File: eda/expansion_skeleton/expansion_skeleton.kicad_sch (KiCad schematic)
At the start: 2 parts

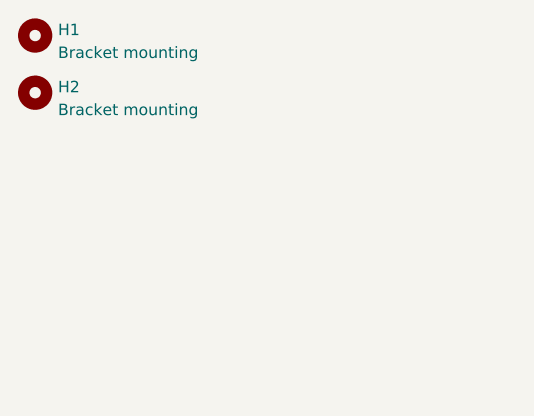
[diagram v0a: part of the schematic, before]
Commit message: EDA work for new expansion header
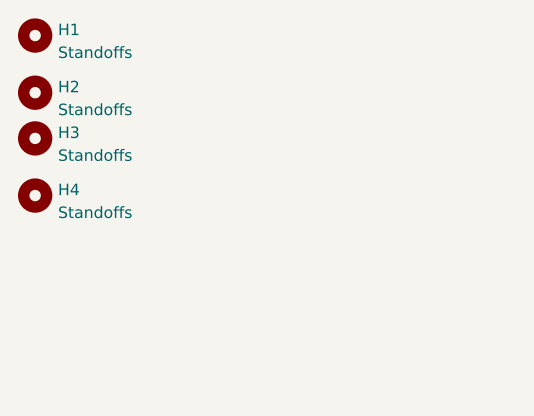
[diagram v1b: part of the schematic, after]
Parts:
- added H3, H4: Standoffs, MountingHole:MountingHole_2.5mm, symbol Mechanical:MountingHole
- H1, H2: value Bracket mounting -> Standoffs
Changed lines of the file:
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@@
 (kicad_sch (version 20230121) (generator eeschema)
   (paper "A4")
+  (symbol (lib_id "Mechanical:MountingHole") (at 21.59 34.29 0) (unit 1)
+    (in_bom yes) (on_board yes) (dnp no) (fields_autoplaced)
+    (property "Reference" "H3" (at 24.13 33.655 0)
+      (effects (font (size 1.27 1.27)) (justify left))
+    )
+    (property "Value" "Standoffs" (at 24.13 36.195 0)
+      (effects (font (size 1.27 1.27)) (justify left))
+    )
+    (property "Footprint" "MountingHole:MountingHole_2.5mm" (at 21.59 34.29 0)
+      (effects (font (size 1.27 1.27)) hide)
+    )
+    (property "Datasheet" "~" (at 21.59 34.29 0)
+      (effects (font (size 1.27 1.27)) hide)
+    )
+    (instances
+      (project "expansion_skeleton"
+        (path "/f65326c0-118f-43ae-8d7d-86cc11609fcf"
+          (reference "H3") (unit 1)
+        )
+      )
+    )
+  )
+  (symbol (lib_id "Mechanical:MountingHole") (at 21.59 40.64 0) (unit 1)
+    (in_bom yes) (on_board yes) (dnp no) (fields_autoplaced)
+    (property "Reference" "H4" (at 24.13 40.005 0)
+      (effects (font (size 1.27 1.27)) (justify left))
+    )
+    (property "Value" "Standoffs" (at 24.13 42.545 0)
+      (effects (font (size 1.27 1.27)) (justify left))
+    )
+    (property "Footprint" "MountingHole:MountingHole_2.5mm" (at 21.59 40.64 0)
+      (effects (font (size 1.27 1.27)) hide)
+    )
+    (property "Datasheet" "~" (at 21.59 40.64 0)
+      (effects (font (size 1.27 1.27)) hide)
+    )
+    (instances
+      (project "expansion_skeleton"
+        (path "/f65326c0-118f-43ae-8d7d-86cc11609fcf"
+          (reference "H4") (unit 1)
+        )
+      )
+    )
+  )
   (symbol (lib_id "Mechanical:MountingHole") (at 21.59 22.86 0) (unit 1)
     (in_bom yes) (on_board yes) (dnp no) (fields_autoplaced)
@@
       (effects (font (size 1.27 1.27)) (justify left))
     )
-    (property "Value" "Bracket mounting" (at 24.13 24.765 0)
+    (property "Value" "Standoffs" (at 24.13 24.765 0)
       (effects (font (size 1.27 1.27)) (justify left))
     )
@@
       (effects (font (size 1.27 1.27)) (justify left))
     )
-    (property "Value" "Bracket mounting" (at 24.13 31.115 0)
+    (property "Value" "Standoffs" (at 24.13 31.115 0)
       (effects (font (size 1.27 1.27)) (justify left))
     )

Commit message: Branch of uart to v1
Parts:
- removed H1, H2, H3, H4: Standoffs, MountingHole:MountingHole_2.5mm, symbol Mechanical:MountingHole
- added H1, H2, H3, H4, H5, H6: MountingHole_Pad, MountingHole:MountingHole_2.5mm_Pad_Via, symbol Mechanical:MountingHole_Pad
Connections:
- new net GND: H1.1, H2.1, H3.1, H4.1, H5.1, H6.1
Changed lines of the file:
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@@
 (kicad_sch (version 20230121) (generator eeschema)
   (paper "A4")
-  (symbol (lib_id "Mechanical:MountingHole") (at 21.59 34.29 0) (unit 1)
-    (in_bom yes) (on_board yes) (dnp no) (fields_autoplaced)
-    (property "Reference" "H3" (at 24.13 33.655 0)
-      (effects (font (size 1.27 1.27)) (justify left))
-    )
-    (property "Value" "Standoffs" (at 24.13 36.195 0)
-      (effects (font (size 1.27 1.27)) (justify left))
-    )
-    (property "Footprint" "MountingHole:MountingHole_2.5mm" (at 21.59 34.29 0)
-      (effects (font (size 1.27 1.27)) hide)
-    )
-    (property "Datasheet" "~" (at 21.59 34.29 0)
-      (effects (font (size 1.27 1.27)) hide)
-    )
+  (junction (at 38.608 41.656) (diameter 0) (color 0 0 0 0)
+  )
+  (junction (at 38.608 62.992) (diameter 0) (color 0 0 0 0)
+  )
+  (junction (at 38.608 52.324) (diameter 0) (color 0 0 0 0)
+  )
+  (junction (at 38.608 32.004) (diameter 0) (color 0 0 0 0)
+  )
+  (junction (at 38.608 73.152) (diameter 0) (color 0 0 0 0)
+  )
+  (wire (pts (xy 30.734 21.844) (xy 38.608 21.844))
+    (stroke (width 0) (type default))
+  )
+  (wire (pts (xy 38.608 73.152) (xy 38.608 78.232))
+    (stroke (width 0) (type default))
+  )
+  (wire (pts (xy 38.608 52.324) (xy 38.608 62.992))
+    (stroke (width 0) (type default))
+  )
+  (wire (pts (xy 30.734 32.004) (xy 38.608 32.004))
+    (stroke (width 0) (type default))
+  )
+  (wire (pts (xy 38.608 21.844) (xy 38.608 32.004))
+    (stroke (width 0) (type default))
+  )
+  (wire (pts (xy 30.48 52.324) (xy 38.608 52.324))
+    (stroke (width 0) (type default))
+  )
+  (wire (pts (xy 38.608 32.004) (xy 38.608 41.656))
+    (stroke (width 0) (type default))
+  )
+  (wire (pts (xy 38.608 62.992) (xy 38.608 73.152))
+    (stroke (width 0) (type default))
+  )
+  (wire (pts (xy 38.608 41.656) (xy 38.608 52.324))
+    (stroke (width 0) (type default))
+  )
+  (wire (pts (xy 30.226 62.992) (xy 38.608 62.992))
+    (stroke (width 0) (type default))
+  )
+  (wire (pts (xy 30.226 73.152) (xy 38.608 73.152))
+    (stroke (width 0) (type default))
+  )
+  (wire (pts (xy 30.226 41.656) (xy 38.608 41.656))
+    (stroke (width 0) (type default))
+  )
+  (symbol (lib_id "Mechanical:MountingHole_Pad") (at 28.194 21.844 90) (unit 1)
+    (in_bom yes) (on_board yes) (dnp no) (fields_autoplaced)
+    (property "Reference" "H1" (at 26.924 15.748 90)
+      (effects (font (size 1.27 1.27)))
+    )
+    (property "Value" "MountingHole_Pad" (at 26.924 18.288 90)
+      (effects (font (size 1.27 1.27)))
+    )
+    (property "Footprint" "MountingHole:MountingHole_2.5mm_Pad_Via" (at 28.194 21.844 0)
+      (effects (font (size 1.27 1.27)) hide)
+    )
+    (property "Datasheet" "~" (at 28.194 21.844 0)
+      (effects (font (size 1.27 1.27)) hide)
+    )
+    (pin "1")
+    (instances
+      (project "expansion_skeleton"
+        (path "/f65326c0-118f-43ae-8d7d-86cc11609fcf"
+          (reference "H1") (unit 1)
+        )
+      )
+    )
+  )
+  (symbol (lib_id "Mechanical:MountingHole_Pad") (at 28.194 32.004 90) (unit 1)
+    (in_bom yes) (on_board yes) (dnp no) (fields_autoplaced)
+    (property "Reference" "H2" (at 26.924 25.908 90)
+      (effects (font (size 1.27 1.27)))
+    )
+    (property "Value" "MountingHole_Pad" (at 26.924 28.448 90)
+      (effects (font (size 1.27 1.27)))
+    )
+    (property "Footprint" "MountingHole:MountingHole_2.5mm_Pad_Via" (at 28.194 32.004 0)
+      (effects (font (size 1.27 1.27)) hide)
+    )
+    (property "Datasheet" "~" (at 28.194 32.004 0)
+      (effects (font (size 1.27 1.27)) hide)
+    )
+    (pin "1")
+    (instances
+      (project "expansion_skeleton"
+        (path "/f65326c0-118f-43ae-8d7d-86cc11609fcf"
+          (reference "H2") (unit 1)
+        )
+      )
+    )
+  )
+  (symbol (lib_id "Mechanical:MountingHole_Pad") (at 27.686 73.152 90) (unit 1)
+    (in_bom yes) (on_board yes) (dnp no) (fields_autoplaced)
+    (property "Reference" "H6" (at 26.416 67.056 90)
+      (effects (font (size 1.27 1.27)))
+    )
+    (property "Value" "MountingHole_Pad" (at 26.416 69.596 90)
+      (effects (font (size 1.27 1.27)))
+    )
+    (property "Footprint" "MountingHole:MountingHole_2.5mm_Pad_Via" (at 27.686 73.152 0)
+      (effects (font (size 1.27 1.27)) hide)
+    )
+    (property "Datasheet" "~" (at 27.686 73.152 0)
+      (effects (font (size 1.27 1.27)) hide)
+    )
+    (pin "1")
+    (instances
+      (project "expansion_skeleton"
+        (path "/f65326c0-118f-43ae-8d7d-86cc11609fcf"
+          (reference "H6") (unit 1)
+        )
+      )
+    )
+  )
+  (symbol (lib_id "Mechanical:MountingHole_Pad") (at 27.686 62.992 90) (unit 1)
+    (in_bom yes) (on_board yes) (dnp no) (fields_autoplaced)
+    (property "Reference" "H5" (at 26.416 56.896 90)
+      (effects (font (size 1.27 1.27)))
+    )
+    (property "Value" "MountingHole_Pad" (at 26.416 59.436 90)
+      (effects (font (size 1.27 1.27)))
+    )
+    (property "Footprint" "MountingHole:MountingHole_2.5mm_Pad_Via" (at 27.686 62.992 0)
+      (effects (font (size 1.27 1.27)) hide)
+    )
+    (property "Datasheet" "~" (at 27.686 62.992 0)
+      (effects (font (size 1.27 1.27)) hide)
+    )
+    (pin "1")
+    (instances
+      (project "expansion_skeleton"
+        (path "/f65326c0-118f-43ae-8d7d-86cc11609fcf"
+          (reference "H5") (unit 1)
+        )
+      )
+    )
+  )
+  (symbol (lib_id "Mechanical:MountingHole_Pad") (at 27.686 41.656 90) (unit 1)
+    (in_bom yes) (on_board yes) (dnp no) (fields_autoplaced)
+    (property "Reference" "H3" (at 26.416 35.56 90)
+      (effects (font (size 1.27 1.27)))
+    )
+    (property "Value" "MountingHole_Pad" (at 26.416 38.1 90)
+      (effects (font (size 1.27 1.27)))
+    )
+    (property "Footprint" "MountingHole:MountingHole_2.5mm_Pad_Via" (at 27.686 41.656 0)
+      (effects (font (size 1.27 1.27)) hide)
+    )
+    (property "Datasheet" "~" (at 27.686 41.656 0)
+      (effects (font (size 1.27 1.27)) hide)
+    )
+    (pin "1")
     (instances
       (project "expansion_skeleton"
@@
     )
   )
-  (symbol (lib_id "Mechanical:MountingHole") (at 21.59 40.64 0) (unit 1)
-    (in_bom yes) (on_board yes) (dnp no) (fields_autoplaced)
-    (property "Reference" "H4" (at 24.13 40.005 0)
-      (effects (font (size 1.27 1.27)) (justify left))
-    )
-    (property "Value" "Standoffs" (at 24.13 42.545 0)
-      (effects (font (size 1.27 1.27)) (justify left))
-    )
-    (property "Footprint" "MountingHole:MountingHole_2.5mm" (at 21.59 40.64 0)
-      (effects (font (size 1.27 1.27)) hide)
-    )
-    (property "Datasheet" "~" (at 21.59 40.64 0)
-      (effects (font (size 1.27 1.27)) hide)
-    )
+  (symbol (lib_id "Mechanical:MountingHole_Pad") (at 27.94 52.324 90) (unit 1)
+    (in_bom yes) (on_board yes) (dnp no) (fields_autoplaced)
+    (property "Reference" "H4" (at 26.67 46.228 90)
+      (effects (font (size 1.27 1.27)))
+    )
+    (property "Value" "MountingHole_Pad" (at 26.67 48.768 90)
+      (effects (font (size 1.27 1.27)))
+    )
+    (property "Footprint" "MountingHole:MountingHole_2.5mm_Pad_Via" (at 27.94 52.324 0)
+      (effects (font (size 1.27 1.27)) hide)
+    )
+    (property "Datasheet" "~" (at 27.94 52.324 0)
+      (effects (font (size 1.27 1.27)) hide)
+    )
+    (pin "1")
     (instances
       (project "expansion_skeleton"
@@
     )
   )
-  (symbol (lib_id "Mechanical:MountingHole") (at 21.59 22.86 0) (unit 1)
-    (in_bom yes) (on_board yes) (dnp no) (fields_autoplaced)
-    (property "Reference" "H1" (at 24.13 22.225 0)
-      (effects (font (size 1.27 1.27)) (justify left))
-    )
-    (property "Value" "Standoffs" (at 24.13 24.765 0)
-      (effects (font (size 1.27 1.27)) (justify left))
-    )
-    (property "Footprint" "MountingHole:MountingHole_2.5mm" (at 21.59 22.86 0)
-      (effects (font (size 1.27 1.27)) hide)
-    )
-    (property "Datasheet" "~" (at 21.59 22.86 0)
-      (effects (font (size 1.27 1.27)) hide)
-    )
-    (instances
-      (project "expansion_skeleton"
-        (path "/f65326c0-118f-43ae-8d7d-86cc11609fcf"
-          (reference "H1") (unit 1)
-        )
-      )
-    )
-  )
-  (symbol (lib_id "Mechanical:MountingHole") (at 21.59 29.21 0) (unit 1)
-    (in_bom yes) (on_board yes) (dnp no) (fields_autoplaced)
-    (property "Reference" "H2" (at 24.13 28.575 0)
-      (effects (font (size 1.27 1.27)) (justify left))
-    )
-    (property "Value" "Standoffs" (at 24.13 31.115 0)
-      (effects (font (size 1.27 1.27)) (justify left))
-    )
-    (property "Footprint" "MountingHole:MountingHole_2.5mm" (at 21.59 29.21 0)
-      (effects (font (size 1.27 1.27)) hide)
-    )
-    (property "Datasheet" "~" (at 21.59 29.21 0)
-      (effects (font (size 1.27 1.27)) hide)
-    )
-    (instances
-      (project "expansion_skeleton"
-        (path "/f65326c0-118f-43ae-8d7d-86cc11609fcf"
-          (reference "H2") (unit 1)
-        )
-      )
+  (symbol (lib_id "power:GND") (at 38.608 78.232 0) (unit 1)
+    (in_bom yes) (on_board yes) (dnp no) (fields_autoplaced)
+    (property "Reference" "#PWR01" (at 38.608 84.582 0)
+      (effects (font (size 1.27 1.27)) hide)
+    )
+    (property "Value" "GND" (at 38.608 83.82 0)
+      (effects (font (size 1.27 1.27)))
+    )
+    (property "Footprint" "" (at 38.608 78.232 0)
+      (effects (font (size 1.27 1.27)) hide)
+    )
+    (property "Datasheet" "" (at 38.608 78.232 0)
+      (effects (font (size 1.27 1.27)) hide)
+    )
+    (pin "1")
+    (instances
+      (project "expansion_skeleton"
+        (path "/f65326c0-118f-43ae-8d7d-86cc11609fcf"
+          (reference "#PWR01") (unit 1)
+        )
+      )
